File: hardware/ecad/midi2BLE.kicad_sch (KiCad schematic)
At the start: 0 parts

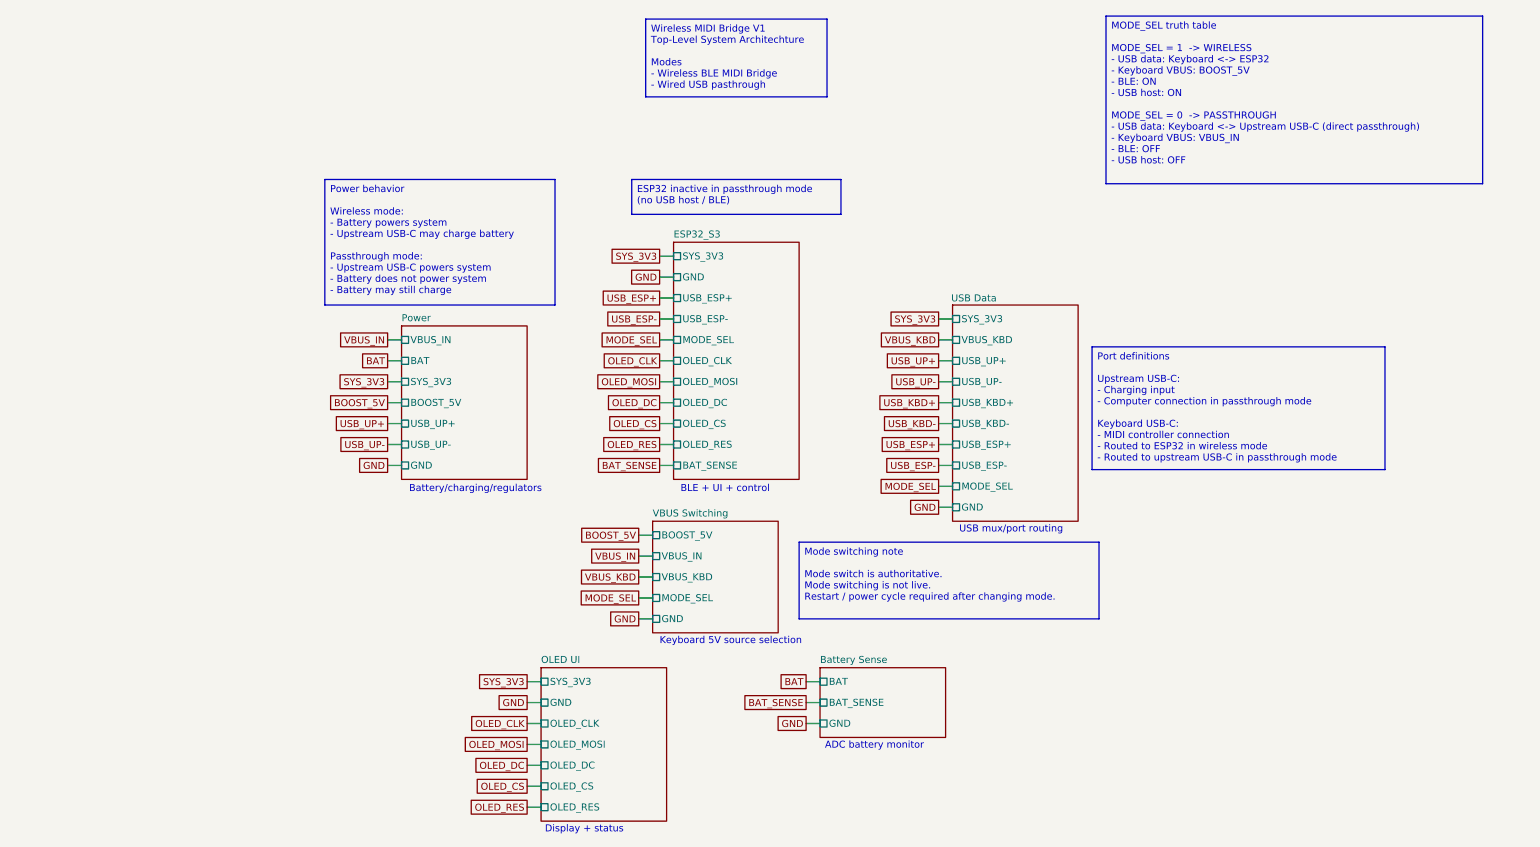
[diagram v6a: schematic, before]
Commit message: fix: resolve fatal power and USB switching errors
Replace TLV61047 boost converter with MT3608; add SS14 catch diode, 4.7µH inductor, and correct FB divider (180kΩ/51kΩ) for 5V output
Fix TPS62162DSG EN circular dependency; connect directly to U1_OUT
Fix TPS62162DSG FB pin; disconnect from SYS_3V3 and tie to GND
Fix TPS2116 power mux; remove series resistor on VIN1, add correct PR1 divider (100kΩ/27kΩ), tie MODE to VIN1 for priority mode
Fix TS3USB30E OE pin; tie directly to GND to keep switch always enabled
Add PGOOD pull-up resistor (10kΩ) to SYS_3V3 on BQ24079
Change ISET resistor from 590Ω to 680Ω for 1.3A charge current
Remove unnecessary R5 (10kΩ VBUS_IN to GND bleed resistor)
Add USB_STATUS net from TPS2116 ST pin to ESP32 IO38
Add PWR_FLAG to BOOST_5V and U1_OUT nets
Fix U1_PGOOD net label placement; separate from SYS_3V3 pull-up node
Add documentation boxes and truth tables to power and USB switching pages
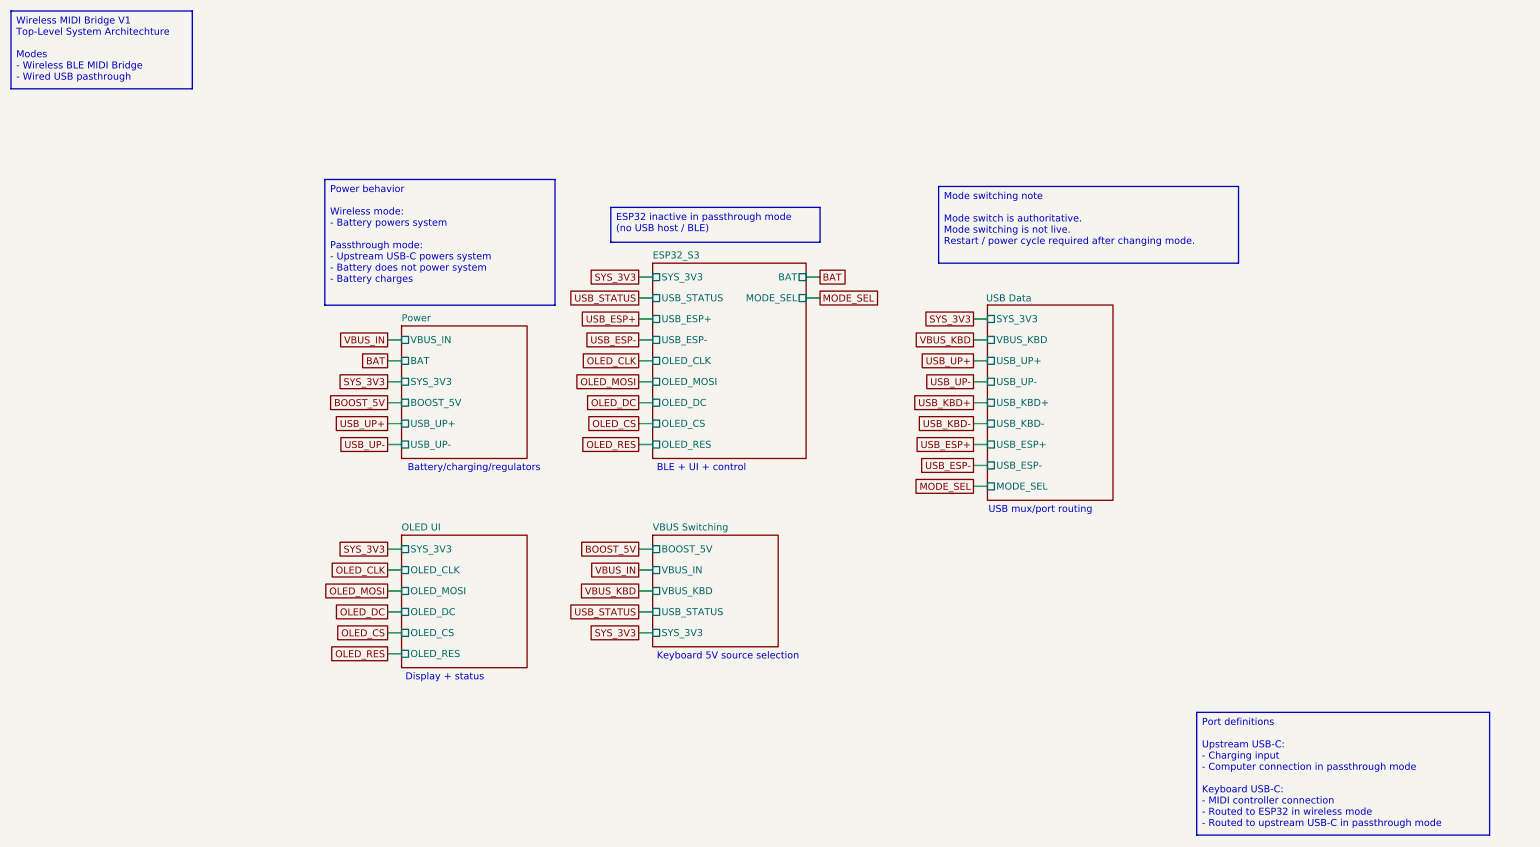
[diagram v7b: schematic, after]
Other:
- removed sheet Battery Sense
- sheet ESP32_S3 ports: added BAT, USB_STATUS; removed BAT_SENSE, GND
- sheet OLED UI ports: added none; removed GND
- sheet Power ports: added none; removed GND
- sheet USB Data ports: added none; removed GND
- sheet VBUS Switching ports: added SYS_3V3, USB_STATUS; removed GND, MODE_SEL
- note removed: "ADC battery monitor"
